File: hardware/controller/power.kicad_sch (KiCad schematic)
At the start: 5 parts, among them J10 Conn_01x04_Pin, J11 Barrel_Jack, J7 Conn_01x04_Pin, J8 Conn_01x04_Pin, J9 Conn_01x04_Pin

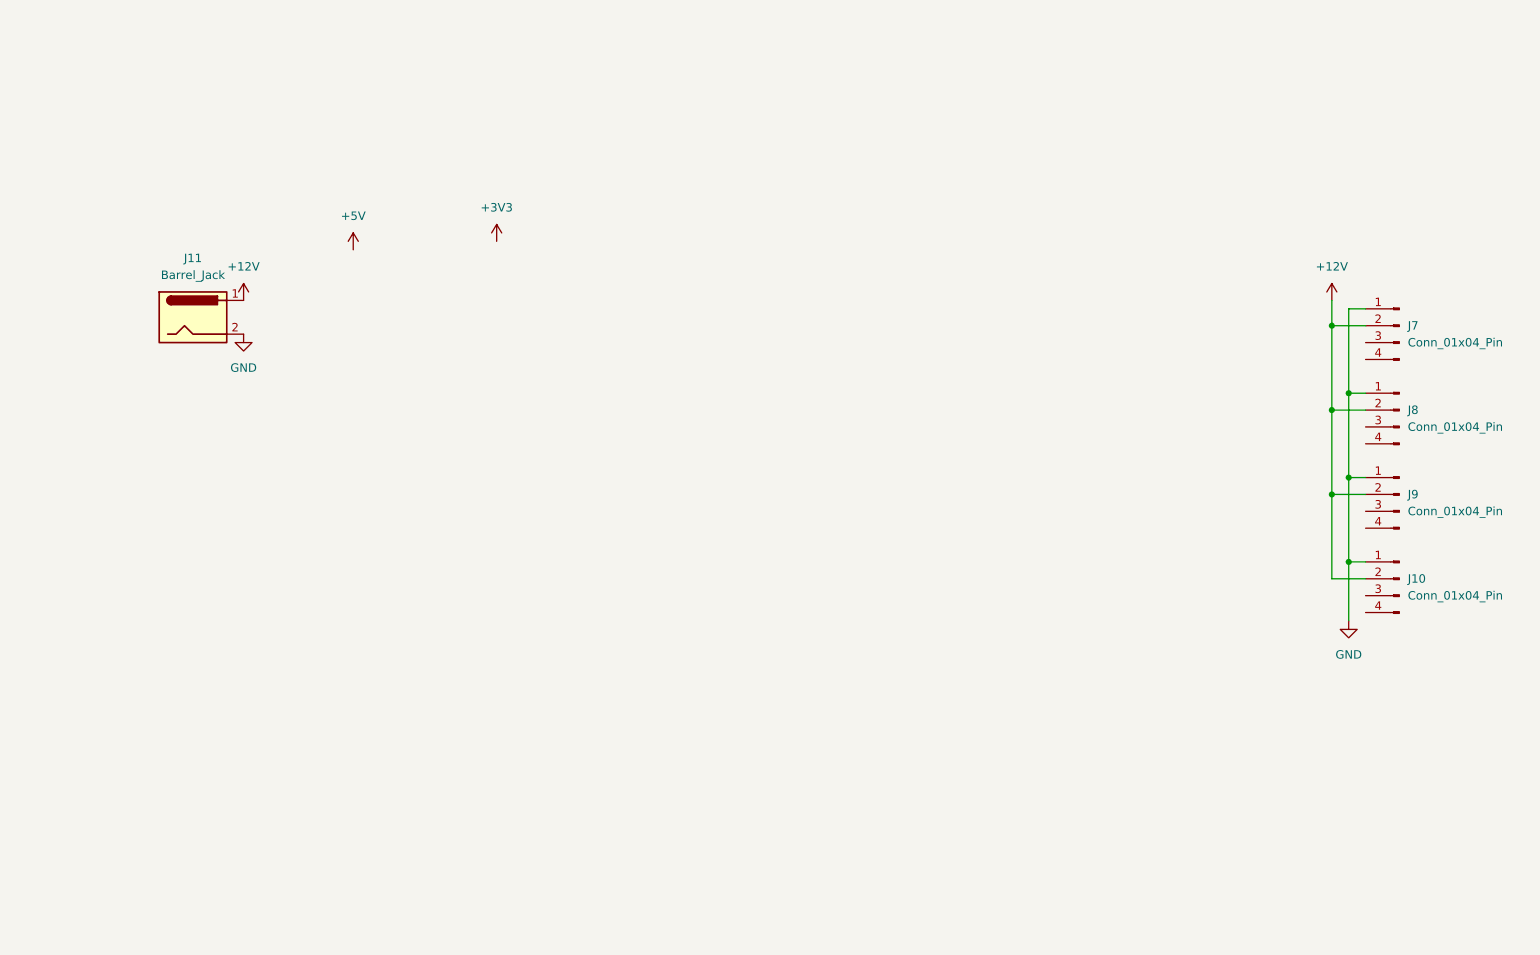
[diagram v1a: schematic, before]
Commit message: Filled out power section of schematic
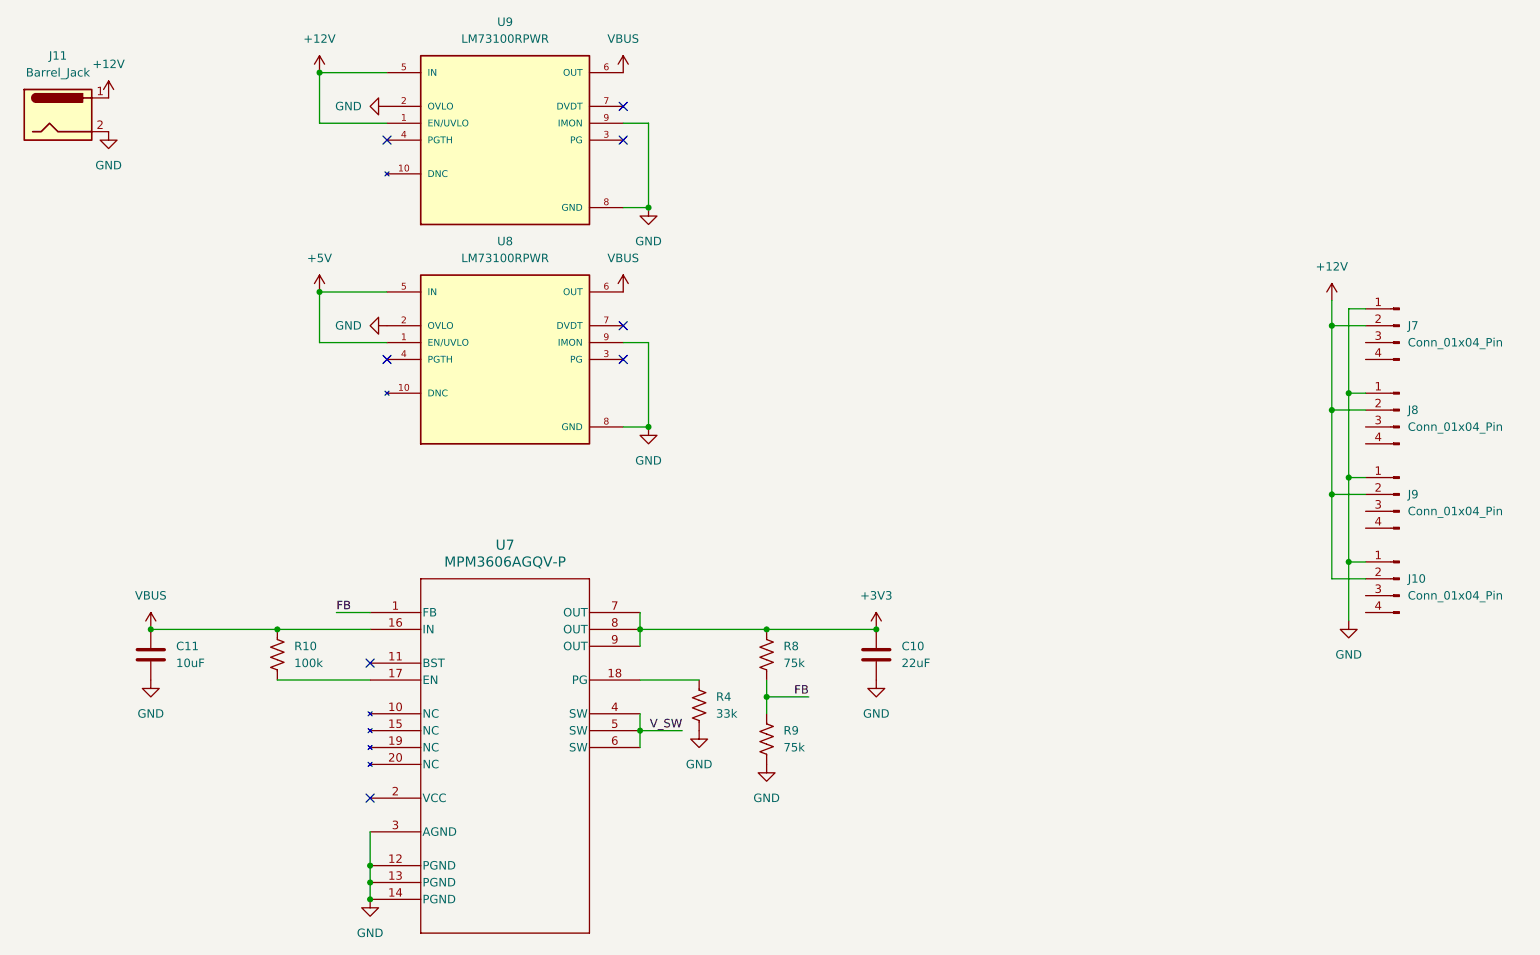
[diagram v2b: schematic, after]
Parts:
- added C10: 22uF, Capacitor_SMD:C_0805_2012Metric, symbol Device:C
- added C11: 10uF, Capacitor_SMD:C_0805_2012Metric, symbol Device:C
- added R10: 100k, Resistor_SMD:R_0805_2012Metric, symbol Device:R_US
- added R4: 33k, Resistor_SMD:R_0805_2012Metric, symbol Device:R_US
- added R8, R9: 75k, Resistor_SMD:R_0805_2012Metric, symbol Device:R_US
- added U7: MPM3606AGQV-P, MPM3606:QFN3p0x5p0x1p6_MPM3606A_MNP, symbol MPM3606:MPM3606AGQV-P
- added U8, U9: LM73100RPWR, LM73100:IC_LM73100RPWR, symbol LM73100:LM73100RPWR
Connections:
- net +12V: now also U9.1 (EN/UVLO), U9.5 (IN)
- net +3V3: now also C10.1, R8.1, U7.7 (OUT), U7.8 (OUT), U7.9 (OUT)
- net +5V: now also U8.1 (EN/UVLO), U8.5 (IN)
- net GND: now also C10.2, C11.2, R4.2, R9.2, U7.12 (PGND), U7.13 (PGND), U7.14 (PGND), U7.3 (AGND), U8.2 (OVLO), U8.8 (GND), U8.9 (IMON), U9.2 (OVLO), U9.8 (GND), U9.9 (IMON)
- new net: R10.2, U7.17 (EN)
- new net: R4.1, U7.18 (PG)
- new net FB: R8.2, R9.1, U7.1 (FB)
- new net VBUS: C11.1, R10.1, U7.16 (IN), U8.6 (OUT), U9.6 (OUT)
- new net V_SW: U7.4 (SW), U7.5 (SW), U7.6 (SW)
- no-connect marks 0 -> 8
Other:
- moved on the sheet: J11

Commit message: Fix USB symbol, adjust decoupling caps
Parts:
- added TP1, TP2, TP3: TestPoint, TestPoint:TestPoint_Pad_D2.0mm, symbol Connector:TestPoint
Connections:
- net +3V3: now also TP2.1
- net GND: now also TP3.1
- net VBUS: now also TP1.1
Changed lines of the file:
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@@
+	)
+	(junction
+		(at 55.88 115.57)
+		(diameter 0)
+		(color 0 0 0 0)
 	)
 	(junction
@@
 	)
 	(junction
+		(at 78.74 146.05)
+		(diameter 0)
+		(color 0 0 0 0)
+	)
+	(junction
 		(at 119.38 130.81)
 		(diameter 0)
@@
 		(color 0 0 0 0)
 	)
+	(junction
+		(at 128.27 115.57)
+		(diameter 0)
+		(color 0 0 0 0)
+	)
 	(no_connect
 		(at 116.84 36.83)
@@
 	(wire
 		(pts
-			(xy 45.72 115.57) (xy 64.77 115.57)
+			(xy 45.72 115.57) (xy 55.88 115.57)
 		)
 		(stroke
@@
 	(wire
 		(pts
+			(xy 128.27 115.57) (xy 138.43 115.57)
+		)
+		(stroke
+			(width 0)
+			(type default)
+		)
+	)
+	(wire
+		(pts
 			(xy 120.65 85.09) (xy 116.84 85.09)
 		)
@@
 	(wire
 		(pts
-			(xy 119.38 115.57) (xy 138.43 115.57)
+			(xy 119.38 115.57) (xy 128.27 115.57)
 		)
 		(stroke
@@
 		(pts
 			(xy 223.52 95.25) (xy 228.6 95.25)
+		)
+		(stroke
+			(width 0)
+			(type default)
+		)
+	)
+	(wire
+		(pts
+			(xy 55.88 115.57) (xy 64.77 115.57)
 		)
 		(stroke
@@
 	)
 	(symbol
+		(lib_id "Connector:TestPoint")
+		(at 128.27 115.57 0)
+		(unit 1)
+		(exclude_from_sim no)
+		(in_bom yes)
+		(on_board yes)
+		(dnp no)
+		(fields_autoplaced yes)
+		(property "Reference" "TP2"
+			(at 130.81 110.9979 0)
+			(effects
+				(font
+					(size 1.27 1.27)
+				)
+				(justify left)
+			)
+		)
+		(property "Value" "TestPoint"
+			(at 130.81 113.5379 0)
+			(effects
+				(font
+					(size 1.27 1.27)
+				)
+				(justify left)
+			)
+		)
+		(property "Footprint" "TestPoint:TestPoint_Pad_D2.0mm"
+			(at 133.35 115.57 0)
+			(effects
+				(font
+					(size 1.27 1.27)
+				)
+				(hide yes)
+			)
+		)
+		(property "Datasheet" "~"
+			(at 133.35 115.57 0)
+			(effects
+				(font
+					(size 1.27 1.27)
+				)
+				(hide yes)
+			)
+		)
+		(property "Description" "test point"
+			(at 128.27 115.57 0)
+			(effects
+				(font
+					(size 1.27 1.27)
+				)
+				(hide yes)
+			)
+		)
+		(pin "1"
+		)
+		(instances
+			(project "controller"
+				(path "/3ee12552-bbaf-4643-8241-99077a41063f/dc443349-7fb4-42c6-a18e-09a219bb9ecd"
+					(reference "TP2")
+					(unit 1)
+				)
+			)
+		)
+	)
+	(symbol
 		(lib_id "power:GND")
 		(at 154.94 123.19 0)
@@
 				(path "/3ee12552-bbaf-4643-8241-99077a41063f/dc443349-7fb4-42c6-a18e-09a219bb9ecd"
 					(reference "#PWR045")
+					(unit 1)
+				)
+			)
+		)
+	)
+	(symbol
+		(lib_id "Connector:TestPoint")
+		(at 78.74 146.05 90)
+		(unit 1)
+		(exclude_from_sim no)
+		(in_bom yes)
+		(on_board yes)
+		(dnp no)
+		(fields_autoplaced yes)
+		(property "Reference" "TP3"
+			(at 75.438 140.97 90)
+			(effects
+				(font
+					(size 1.27 1.27)
+				)
+			)
+		)
+		(property "Value" "TestPoint"
+			(at 75.438 143.51 90)
+			(effects
+				(font
+					(size 1.27 1.27)
+				)
+			)
+		)
+		(property "Footprint" "TestPoint:TestPoint_Pad_D2.0mm"
+			(at 78.74 140.97 0)
+			(effects
+				(font
+					(size 1.27 1.27)
+				)
+				(hide yes)
+			)
+		)
+		(property "Datasheet" "~"
+			(at 78.74 140.97 0)
+			(effects
+				(font
+					(size 1.27 1.27)
+				)
+				(hide yes)
+			)
+		)
+		(property "Description" "test point"
+			(at 78.74 146.05 0)
+			(effects
+				(font
+					(size 1.27 1.27)
+				)
+				(hide yes)
+			)
+		)
+		(pin "1"
+		)
+		(instances
+			(project "controller"
+				(path "/3ee12552-bbaf-4643-8241-99077a41063f/dc443349-7fb4-42c6-a18e-09a219bb9ecd"
+					(reference "TP3")
 					(unit 1)
 				)
@@
 					(unit 1)
 				)
+			)
+		)
+	)
+	(symbol
+		(lib_id "Connector:TestPoint")
+		(at 55.88 115.57 0)
+		(unit 1)
+		(exclude_from_sim no)
+		(in_bom yes)
+		(on_board yes)
+		(dnp no)
+		(fields_autoplaced yes)
+		(property "Reference" "TP1"
+			(at 58.42 110.9979 0)
+			(effects
+				(font
+					(size 1.27 1.27)
+				)
+				(justify left)
+			)
+		)
+		(property "Value" "TestPoint"
+			(at 58.42 113.5379 0)
+			(effects
+				(font
+					(size 1.27 1.27)
+				)
+				(justify left)
+			)
+		)
+		(property "Footprint" "TestPoint:TestPoint_Pad_D2.0mm"
+			(at 60.96 115.57 0)
+			(effects
+				(font
+					(size 1.27 1.27)
+				)
+				(hide yes)
+			)
+		)
+		(property "Datasheet" "~"
+			(at 60.96 115.57 0)
+			(effects
+				(font
+					(size 1.27 1.27)
+				)
+				(hide yes)
+			)
+		)
+		(property "Description" "test point"
+			(at 55.88 115.57 0)
+			(effects
+				(font
+					(size 1.27 1.27)
+				)
+				(hide yes)
+			)
+		)
+		(pin "1"
+		)
+		(instances
+			(project ""
+				(path "/3ee12552-bbaf-4643-8241-99077a41063f/dc443349-7fb4-42c6-a18e-09a219bb9ecd"
+					(reference "TP1")
+					(unit 1)
+				)

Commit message: Drop to 3x thermocouples, 2x fans
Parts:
- removed J10, J9: Conn_01x04_Pin, Connector:FanPinHeader_1x04_P2.54mm_Vertical, symbol Connector:Conn_01x04_Pin
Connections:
- net FAN_1_TACH: now reaches J8.3 (Pin_3)
- net FAN_0_TACH: now reaches J7.3 (Pin_3)
- no-connect marks 8 -> 10
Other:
- moved on the sheet: J7, J8

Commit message: Add more decoupling caps
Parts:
- added C2: 10uF, Capacitor_SMD:C_0805_2012Metric, symbol Device:C
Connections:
- net +12V: now also C2.1
- net GND: now also C2.2
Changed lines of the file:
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@@
+	(symbol
+		(lib_id "power:GND")
+		(at 53.34 41.91 0)
+		(unit 1)
+		(exclude_from_sim no)
+		(in_bom yes)
+		(on_board yes)
+		(dnp no)
+		(fields_autoplaced yes)
+		(property "Reference" "#PWR012"
+			(at 53.34 48.26 0)
+			(effects
+				(font
+					(size 1.27 1.27)
+				)
+				(hide yes)
+			)
+		)
+		(property "Value" "GND"
+			(at 53.34 46.99 0)
+			(effects
+				(font
+					(size 1.27 1.27)
+				)
+			)
+		)
+		(property "Footprint" ""
+			(at 53.34 41.91 0)
+			(effects
+				(font
+					(size 1.27 1.27)
+				)
+				(hide yes)
+			)
+		)
+		(property "Datasheet" ""
+			(at 53.34 41.91 0)
+			(effects
+				(font
+					(size 1.27 1.27)
+				)
+				(hide yes)
+			)
+		)
+		(property "Description" "Power symbol creates a global label with name \"GND\" , ground"
+			(at 53.34 41.91 0)
+			(effects
+				(font
+					(size 1.27 1.27)
+				)
+				(hide yes)
+			)
+		)
+		(pin "1"
+		)
+		(instances
+			(project "controller"
+				(path "/3ee12552-bbaf-4643-8241-99077a41063f/dc443349-7fb4-42c6-a18e-09a219bb9ecd"
+					(reference "#PWR012")
+					(unit 1)
+				)
+			)
+		)
+	)
 	(symbol
 		(lib_id "power:GND")
@@
 	)
 	(symbol
+		(lib_id "Device:C")
+		(at 53.34 38.1 0)
+		(unit 1)
+		(exclude_from_sim no)
+		(in_bom yes)
+		(on_board yes)
+		(dnp no)
+		(fields_autoplaced yes)
+		(property "Reference" "C2"
+			(at 57.15 36.8299 0)
+			(effects
+				(font
+					(size 1.27 1.27)
+				)
+				(justify left)
+			)
+		)
+		(property "Value" "10uF"
+			(at 57.15 39.3699 0)
+			(effects
+				(font
+					(size 1.27 1.27)
+				)
+				(justify left)
+			)
+		)
+		(property "Footprint" "Capacitor_SMD:C_0805_2012Metric"
+			(at 54.3052 41.91 0)
+			(effects
+				(font
+					(size 1.27 1.27)
+				)
+				(hide yes)
+			)
+		)
+		(property "Datasheet" "~"
+			(at 53.34 38.1 0)
+			(effects
+				(font
+					(size 1.27 1.27)
+				)
+				(hide yes)
+			)
+		)
+		(property "Description" "Unpolarized capacitor"
+			(at 53.34 38.1 0)
+			(effects
+				(font
+					(size 1.27 1.27)
+				)
+				(hide yes)
+			)
+		)
+		(pin "1"
+		)
+		(pin "2"
+		)
+		(instances
+			(project "controller"
+				(path "/3ee12552-bbaf-4643-8241-99077a41063f/dc443349-7fb4-42c6-a18e-09a219bb9ecd"
+					(reference "C2")
+					(unit 1)
+				)
+			)
+		)
+	)
+	(symbol
 		(lib_id "power:+12V")
 		(at 39.37 35.56 0)
@@
 					(unit 1)
 				)
+			)
+		)
+	)
+	(symbol
+		(lib_id "power:+12V")
+		(at 53.34 34.29 0)
+		(unit 1)
+		(exclude_from_sim no)
+		(in_bom yes)
+		(on_board yes)
+		(dnp no)
+		(fields_autoplaced yes)
+		(property "Reference" "#PWR016"
+			(at 53.34 38.1 0)
+			(effects
+				(font
+					(size 1.27 1.27)
+				)
+				(hide yes)
+			)
+		)
+		(property "Value" "+12V"
+			(at 53.34 29.21 0)
+			(effects
+				(font
+					(size 1.27 1.27)
+				)
+			)
+		)
+		(property "Footprint" ""
+			(at 53.34 34.29 0)
+			(effects
+				(font
+					(size 1.27 1.27)
+				)
+				(hide yes)
+			)
+		)
+		(property "Datasheet" ""
+			(at 53.34 34.29 0)
+			(effects
+				(font
+					(size 1.27 1.27)
+				)
+				(hide yes)
+			)
+		)
+		(property "Description" "Power symbol creates a global label with name \"+12V\""
+			(at 53.34 34.29 0)
+			(effects
+				(font
+					(size 1.27 1.27)
+				)
+				(hide yes)
+			)
+		)
+		(pin "1"
+		)
+		(instances
+			(project "controller"
+				(path "/3ee12552-bbaf-4643-8241-99077a41063f/dc443349-7fb4-42c6-a18e-09a219bb9ecd"
+					(reference "#PWR016")
+					(unit 1)
+				)

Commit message: First stab at board routing
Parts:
- TP1, TP2, TP3: footprint TestPoint:TestPoint_Pad_D2.0mm -> TestPoint:TestPoint_THTPad_2.0x2.0mm_Drill1.0mm
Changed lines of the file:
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@@
 			)
 		)
-		(property "Footprint" "TestPoint:TestPoint_Pad_D2.0mm"
+		(property "Footprint" "TestPoint:TestPoint_THTPad_2.0x2.0mm_Drill1.0mm"
 			(at 133.35 115.57 0)
 			(effects
@@
 			)
 		)
-		(property "Footprint" "TestPoint:TestPoint_Pad_D2.0mm"
+		(property "Footprint" "TestPoint:TestPoint_THTPad_2.0x2.0mm_Drill1.0mm"
 			(at 78.74 140.97 0)
 			(effects
@@
 			)
 		)
-		(property "Footprint" "TestPoint:TestPoint_Pad_D2.0mm"
+		(property "Footprint" "TestPoint:TestPoint_THTPad_2.0x2.0mm_Drill1.0mm"
 			(at 60.96 115.57 0)
 			(effects

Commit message: Add LCSC numbers
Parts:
- C10: LCSC (none) -> C602037
- C11, C2: LCSC (none) -> C15850
- R10: LCSC (none) -> C96346
- R4: LCSC (none) -> C17633
- R8, R9: LCSC (none) -> C17819
- U8, U9: LCSC (none) -> C3210761
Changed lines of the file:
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@@
+			)
+		)
+		(property "LCSC" "C3210761"
+			(at 99.06 41.91 0)
+			(effects
+				(font
+					(size 1.27 1.27)
+				)
+				(hide yes)
 			)
 		)
@@
 			)
 		)
+		(property "LCSC" "C96346"
+			(at 64.77 119.38 0)
+			(effects
+				(font
+					(size 1.27 1.27)
+				)
+				(hide yes)
+			)
+		)
 		(pin "2"
 		)
@@
 			)
 		)
+		(property "LCSC" "C602037"
+			(at 154.94 119.38 0)
+			(effects
+				(font
+					(size 1.27 1.27)
+				)
+				(hide yes)
+			)
+		)
 		(pin "2"
 		)
@@
 		)
 		(property "Description" "Resistor, US symbol"
+			(at 128.27 127 0)
+			(effects
+				(font
+					(size 1.27 1.27)
+				)
+				(hide yes)
+			)
+		)
+		(property "LCSC" "C17633"
 			(at 128.27 127 0)
 			(effects
@@
 			)
 		)
+		(property "LCSC" "C15850"
+			(at 53.34 38.1 0)
+			(effects
+				(font
+					(size 1.27 1.27)
+				)
+				(hide yes)
+			)
+		)
 		(pin "1"
 		)
@@
 			)
 		)
+		(property "LCSC" "C15850"
+			(at 45.72 119.38 0)
+			(effects
+				(font
+					(size 1.27 1.27)
+				)
+				(hide yes)
+			)
+		)
 		(pin "1"
 		)
@@
 				)
 				(justify bottom)
+				(hide yes)
+			)
+		)
+		(property "LCSC" "C3210761"
+			(at 99.06 74.93 0)
+			(effects
+				(font
+					(size 1.27 1.27)
+				)
 				(hide yes)
 			)
@@
 			)
 		)
+		(property "LCSC" "C17819"
+			(at 138.43 119.38 0)
+			(effects
+				(font
+					(size 1.27 1.27)
+				)
+				(hide yes)
+			)
+		)
 		(pin "2"
 		)
@@
 			(at 138.43 132.08 0)
 			(effects
+				(font
+					(size 1.27 1.27)
+				)
+				(hide yes)
+			)
+		)
+		(property "LCSC" "C17819"
+			(at 138.43 132.08 0)
+			(effects
